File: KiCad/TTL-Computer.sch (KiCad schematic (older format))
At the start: 0 parts

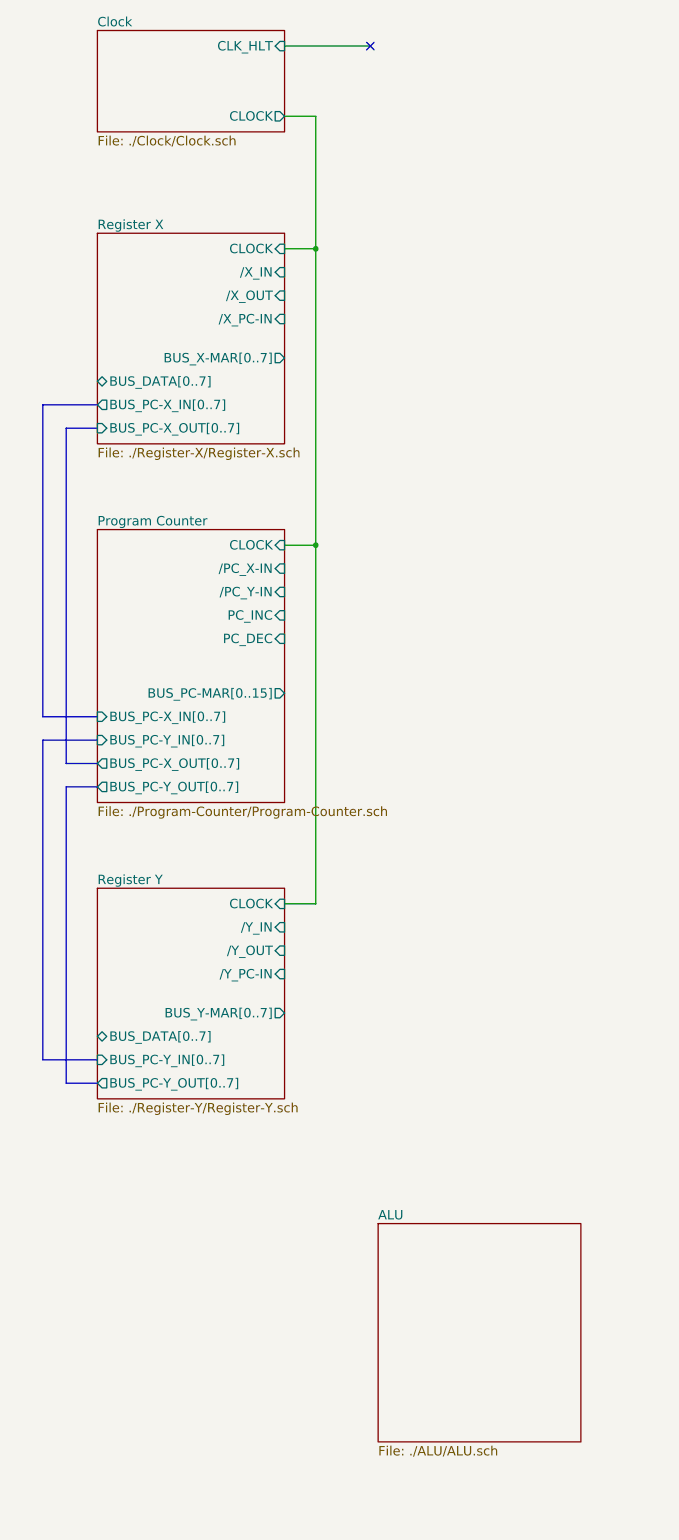
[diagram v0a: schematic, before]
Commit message: Copied X register to Y register
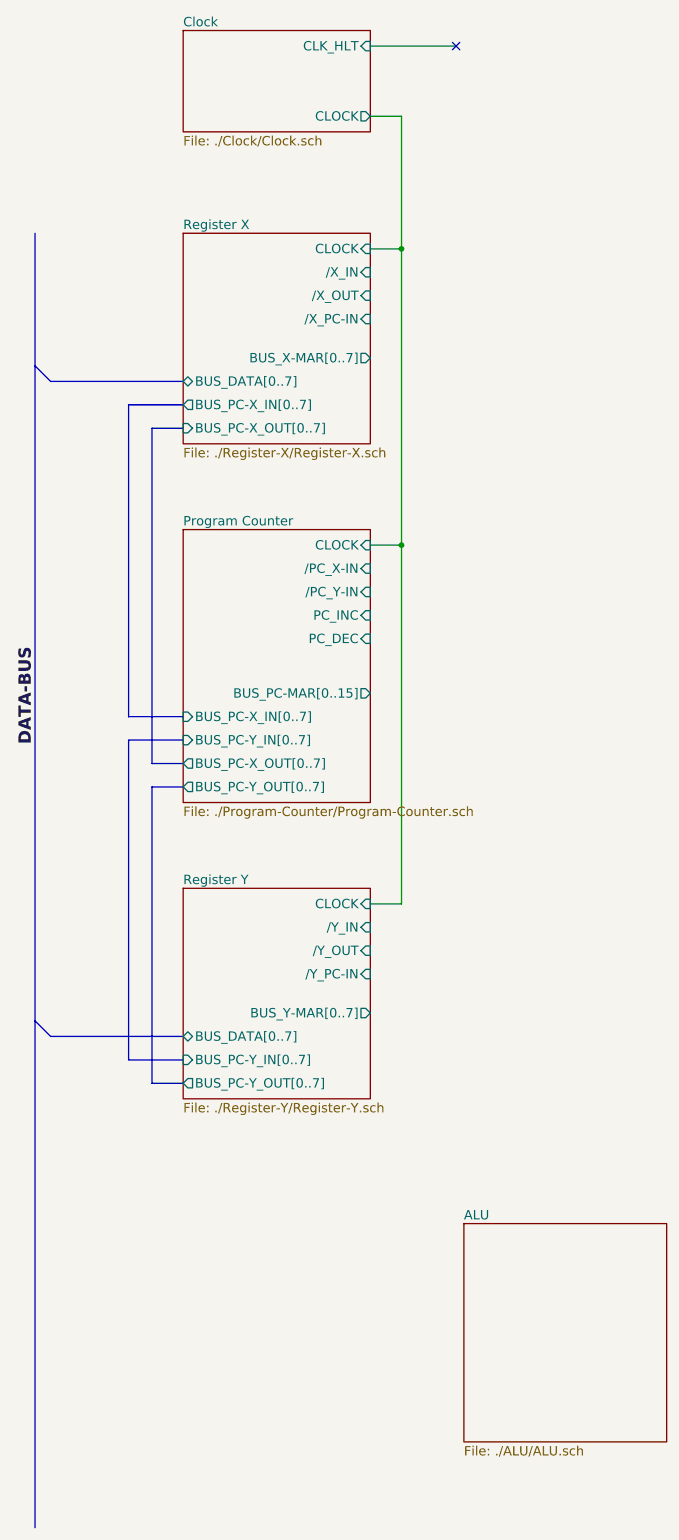
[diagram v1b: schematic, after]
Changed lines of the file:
@@
 $EndDescr
 $Sheet
-S 1100 800  1200 650
+S 1650 800  1200 650
 U 5ACF3206
 F0 "Clock" 60
 F1 "./Clock/Clock.sch" 60
-F2 "CLOCK" O R 2300 1350 60
-F3 "CLK_HLT" I R 2300 900 60
+F2 "CLOCK" O R 2850 1350 60
+F3 "CLK_HLT" I R 2850 900 60
 $EndSheet
 $Sheet
-S 1100 2100 1200 1350
+S 1650 2100 1200 1350
 U 5ACF2F0F
 F0 "Register X" 60
 F1 "./Register-X/Register-X.sch" 60
-F2 "CLOCK" I R 2300 2200 60
-F3 "/X_IN" I R 2300 2350 60
-F4 "/X_OUT" I R 2300 2500 60
-F5 "/X_PC-IN" I R 2300 2650 60
-F6 "BUS_DATA[0..7]" B L 1100 3050 60
-F7 "BUS_PC-X_OUT[0..7]" I L 1100 3350 60
-F8 "BUS_X-MAR[0..7]" O R 2300 2900 60
-F9 "BUS_PC-X_IN[0..7]" O L 1100 3200 60
+F2 "CLOCK" I R 2850 2200 60
+F3 "/X_IN" I R 2850 2350 60
+F4 "/X_OUT" I R 2850 2500 60
+F5 "/X_PC-IN" I R 2850 2650 60
+F6 "BUS_DATA[0..7]" B L 1650 3050 60
+F7 "BUS_PC-X_OUT[0..7]" I L 1650 3350 60
+F8 "BUS_X-MAR[0..7]" O R 2850 2900 60
+F9 "BUS_PC-X_IN[0..7]" O L 1650 3200 60
 $EndSheet
 Wire Bus Line
-	1100 3350 900  3350
+	1650 3350 1450 3350
 Wire Bus Line
-	900  3350 900  5500
+	1450 3350 1450 5500
 Wire Bus Line
-	900  5500 1100 5500
+	1450 5500 1650 5500
 Wire Wire Line
-	2300 1350 2500 1350
+	2850 1350 3050 1350
 Wire Wire Line
-	2500 1350 2500 6400
+	3050 1350 3050 6400
 Wire Wire Line
-	2500 2200 2300 2200
+	3050 2200 2850 2200
 Wire Wire Line
-	2500 4100 2300 4100
-Connection ~ 2500 2200
+	3050 4100 2850 4100
+Connection ~ 3050 2200
 Wire Bus Line
-	1100 3200 750  3200
+	1650 3200 1300 3200
 Wire Bus Line
-	750  3200 750  5200
+	1300 3200 1300 5200
 Wire Bus Line
-	750  5200 1100 5200
-NoConn ~ 2850 900
+	1300 5200 1650 5200
+NoConn ~ 3400 900
 Wire Wire Line
-	2850 900  2300 900
+	3400 900  2850 900
 $Sheet
-S 1100 6300 1200 1350
+S 1650 6300 1200 1350
 U 5AD0848F
 F0 "Register Y" 60
 F1 "./Register-Y/Register-Y.sch" 60
-F2 "BUS_PC-Y_IN[0..7]" I L 1100 7400 60
-F3 "BUS_DATA[0..7]" B L 1100 7250 60
-F4 "CLOCK" I R 2300 6400 60
-F5 "BUS_Y-MAR[0..7]" O R 2300 7100 60
-F6 "/Y_IN" I R 2300 6550 60
-F7 "/Y_OUT" I R 2300 6700 60
-F8 "/Y_PC-IN" I R 2300 6850 60
-F9 "BUS_PC-Y_OUT[0..7]" O L 1100 7550 60
+F2 "BUS_PC-Y_IN[0..7]" I L 1650 7400 60
+F3 "BUS_DATA[0..7]" B L 1650 7250 60
+F4 "CLOCK" I R 2850 6400 60
+F5 "BUS_Y-MAR[0..7]" O R 2850 7100 60
+F6 "/Y_IN" I R 2850 6550 60
+F7 "/Y_OUT" I R 2850 6700 60
+F8 "/Y_PC-IN" I R 2850 6850 60
+F9 "BUS_PC-Y_OUT[0..7]" O L 1650 7550 60
 $EndSheet
 Wire Bus Line
-	1100 5350 750  5350
+	1650 5350 1300 5350
 Wire Bus Line
-	750  5350 750  7400
+	1300 5350 1300 7400
 Wire Bus Line
-	750  7400 1100 7400
+	1300 7400 1650 7400
 Wire Bus Line
-	1100 5650 900  5650
+	1650 5650 1450 5650
 Wire Bus Line
-	900  5650 900  7550
+	1450 5650 1450 7550
 Wire Bus Line
-	900  7550 1100 7550
+	1450 7550 1650 7550
 $Sheet
-S 1100 4000 1200 1750
+S 1650 4000 1200 1750
 U 5ACF340E
 F0 "Program Counter" 60
 F1 "./Program-Counter/Program-Counter.sch" 60
-F2 "/PC_X-IN" I R 2300 4250 60
-F3 "/PC_Y-IN" I R 2300 4400 60
-F4 "PC_INC" I R 2300 4550 60
-F5 "PC_DEC" I R 2300 4700 60
-F6 "CLOCK" I R 2300 4100 60
-F7 "BUS_PC-X_OUT[0..7]" O L 1100 5500 60
-F8 "BUS_PC-Y_OUT[0..7]" O L 1100 5650 60
-F9 "BUS_PC-MAR[0..15]" O R 2300 5050 60
-F10 "BUS_PC-X_IN[0..7]" I L 1100 5200 60
-F11 "BUS_PC-Y_IN[0..7]" I L 1100 5350 60
+F2 "/PC_X-IN" I R 2850 4250 60
+F3 "/PC_Y-IN" I R 2850 4400 60
+F4 "PC_INC" I R 2850 4550 60
+F5 "PC_DEC" I R 2850 4700 60
+F6 "CLOCK" I R 2850 4100 60
+F7 "BUS_PC-X_OUT[0..7]" O L 1650 5500 60
+F8 "BUS_PC-Y_OUT[0..7]" O L 1650 5650 60
+F9 "BUS_PC-MAR[0..15]" O R 2850 5050 60
+F10 "BUS_PC-X_IN[0..7]" I L 1650 5200 60
+F11 "BUS_PC-Y_IN[0..7]" I L 1650 5350 60
 $EndSheet
 Wire Wire Line
-	2500 6400 2300 6400
-Connection ~ 2500 4100
+	3050 6400 2850 6400
+Connection ~ 3050 4100
 $Sheet
-S 2900 8450 1300 1400
+S 3450 8450 1300 1400
 U 5AD5CFF9
 F0 "ALU" 60
 F1 "./ALU/ALU.sch" 60
 $EndSheet
+Wire Bus Line
+	700  2100 700  10400
+Entry Bus Bus
+	700  7150 800  7250
+Wire Bus Line
+	800  7250 1650 7250
+Entry Bus Bus
+	700  2950 800  3050
+Wire Bus Line
+	800  3050 1650 3050
+Text Label 700  4750 3    79   ~ 16
+DATA-BUS
 $EndSCHEMATC

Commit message: Figured out the truth table for my ALU
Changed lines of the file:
@@
 Connection ~ 3050 4100
 $Sheet
-S 3450 8450 1300 1400
+S 3950 8300 1350 2350
 U 5AD5CFF9
 F0 "ALU" 60
 F1 "./ALU/ALU.sch" 60
+F2 "ALU_Cn" I R 5300 8400 60
+F3 "ALU_M" I R 5300 8550 60
+F4 "BUS_A-ALU[0..7]" I L 3950 10400 60
+F5 "BUS_B-ALU[0..7]" I L 3950 10550 60
+F6 "ALU_S0" I R 5300 8700 60
+F7 "ALU_S1" I R 5300 8850 60
+F8 "ALU_S2" I R 5300 9000 60
+F9 "ALU_S3" I R 5300 9150 60
+F10 "ALU_F-EQ" O L 3950 9450 60
+F11 "ALU_F-LT" O L 3950 9600 60
+F12 "ALU_F-GT" O L 3950 9750 60
+F13 "/ALU_OUT" I R 5300 9300 60
+F14 "BUS_DATA[0..7]" O L 3950 10250 60
+F15 "ALU_F-Z" O L 3950 9900 60
+F16 "ALU_F-C" O L 3950 10050 60
 $EndSheet
 Wire Bus Line

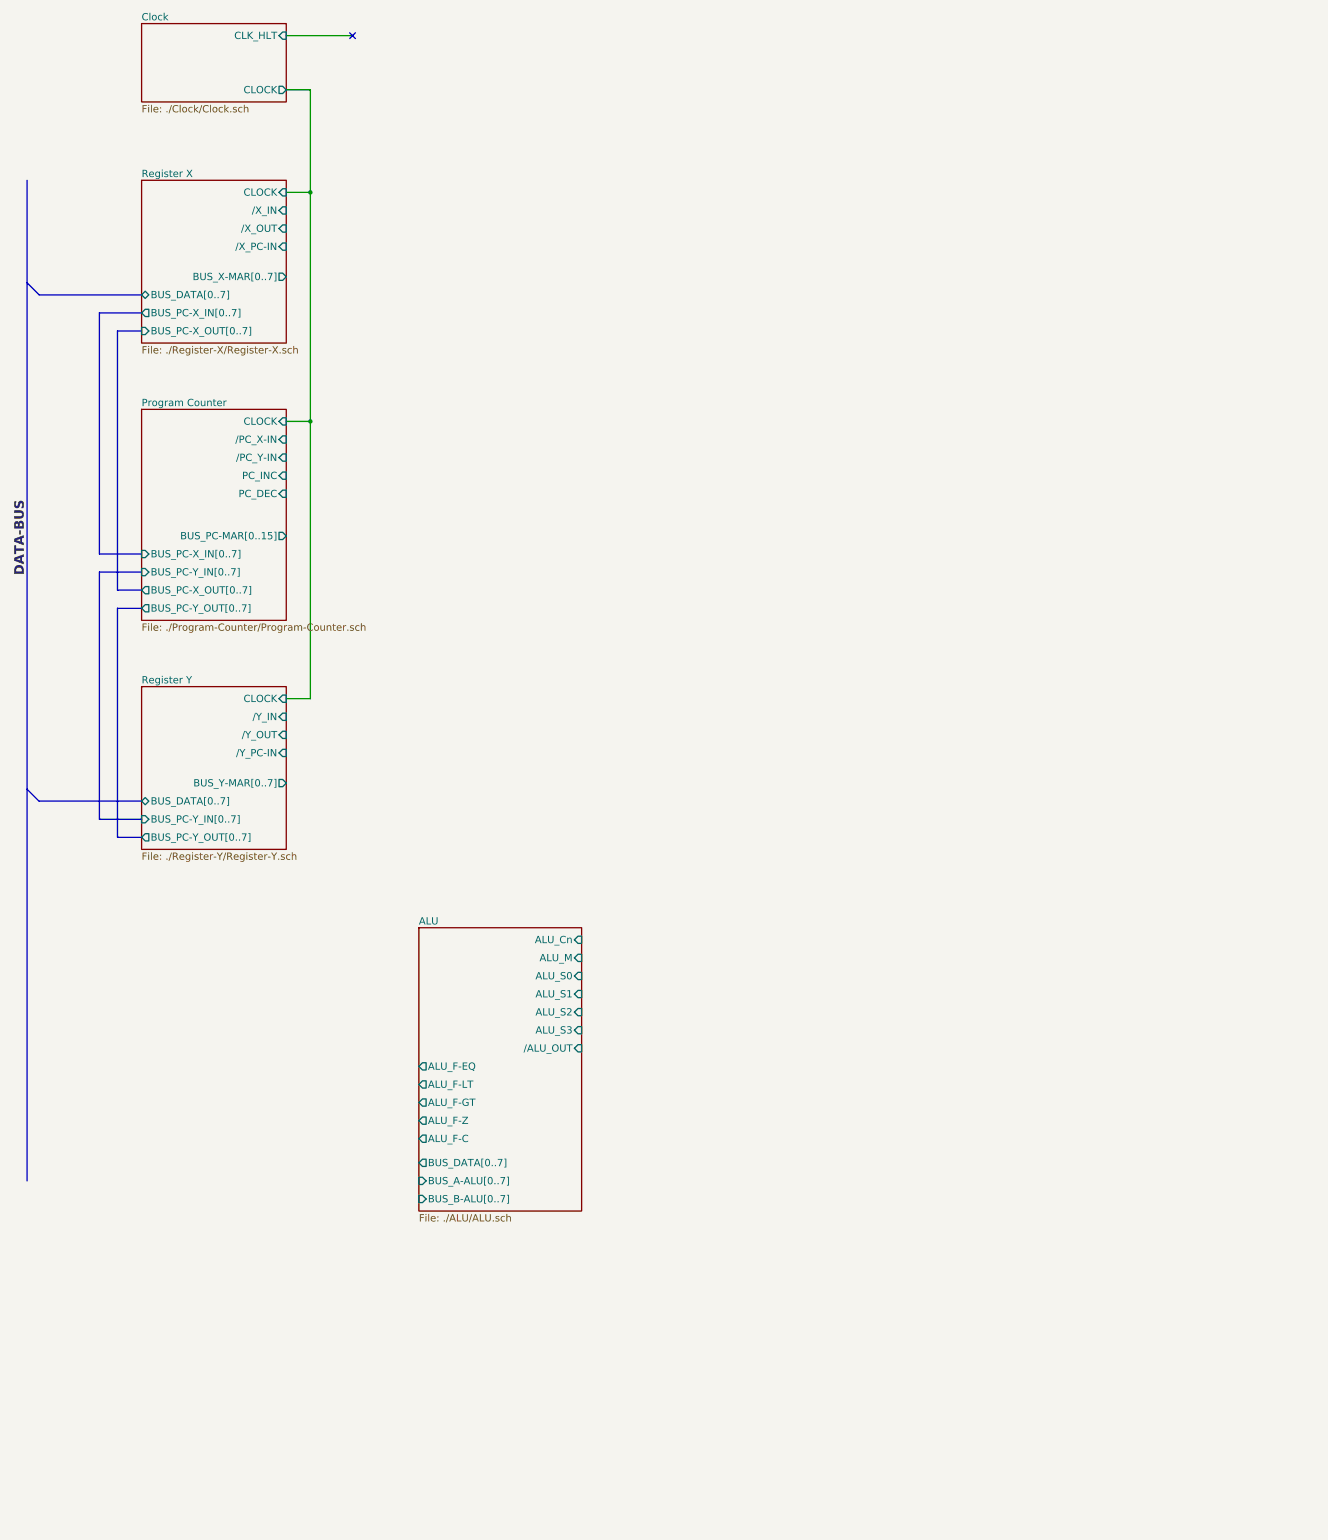
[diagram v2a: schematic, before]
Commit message: Added A and B register schematic
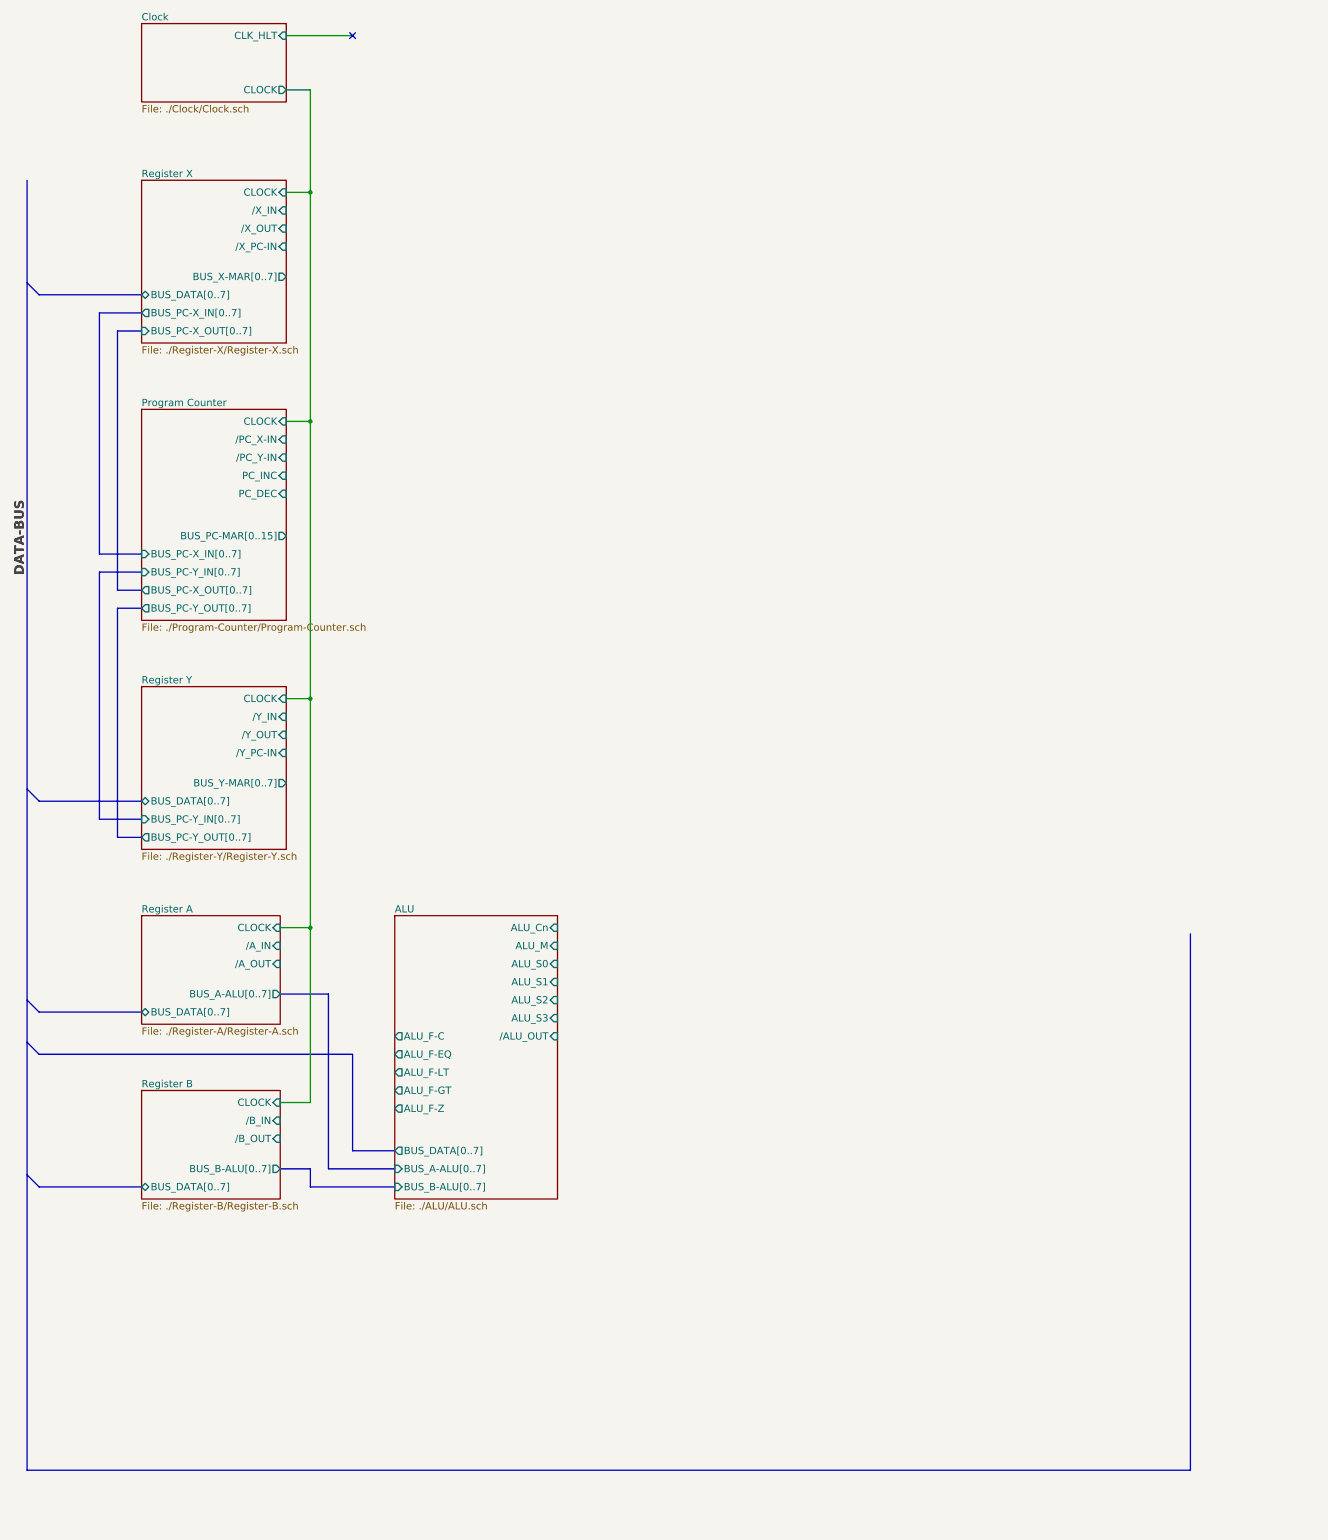
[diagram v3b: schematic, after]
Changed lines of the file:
@@
 $Descr A3 11693 16535 portrait
 encoding utf-8
-Sheet 1 6
+Sheet 1 8
 Title ""
 Date ""
@@
 F9 "BUS_PC-X_IN[0..7]" O L 1650 3200 60
 $EndSheet
-Wire Bus Line
-	1650 3350 1450 3350
-Wire Bus Line
-	1450 3350 1450 5500
-Wire Bus Line
-	1450 5500 1650 5500
-Wire Wire Line
-	2850 1350 3050 1350
-Wire Wire Line
-	3050 1350 3050 6400
-Wire Wire Line
-	3050 2200 2850 2200
-Wire Wire Line
-	3050 4100 2850 4100
-Connection ~ 3050 2200
-Wire Bus Line
-	1650 3200 1300 3200
-Wire Bus Line
-	1300 3200 1300 5200
-Wire Bus Line
-	1300 5200 1650 5200
 NoConn ~ 3400 900
-Wire Wire Line
-	3400 900  2850 900
 $Sheet
 S 1650 6300 1200 1350
@@
 F9 "BUS_PC-Y_OUT[0..7]" O L 1650 7550 60
 $EndSheet
-Wire Bus Line
-	1650 5350 1300 5350
-Wire Bus Line
-	1300 5350 1300 7400
-Wire Bus Line
-	1300 7400 1650 7400
-Wire Bus Line
-	1650 5650 1450 5650
-Wire Bus Line
-	1450 5650 1450 7550
-Wire Bus Line
-	1450 7550 1650 7550
 $Sheet
 S 1650 4000 1200 1750
@@
 F11 "BUS_PC-Y_IN[0..7]" I L 1650 5350 60
 $EndSheet
+$Sheet
+S 3750 8200 1350 2350
+U 5AD5CFF9
+F0 "ALU" 60
+F1 "./ALU/ALU.sch" 60
+F2 "ALU_Cn" I R 5100 8300 60
+F3 "ALU_M" I R 5100 8450 60
+F4 "BUS_A-ALU[0..7]" I L 3750 10300 60
+F5 "BUS_B-ALU[0..7]" I L 3750 10450 60
+F6 "ALU_S0" I R 5100 8600 60
+F7 "ALU_S1" I R 5100 8750 60
+F8 "ALU_S2" I R 5100 8900 60
+F9 "ALU_S3" I R 5100 9050 60
+F10 "ALU_F-EQ" O L 3750 9350 60
+F11 "ALU_F-LT" O L 3750 9500 60
+F12 "ALU_F-GT" O L 3750 9650 60
+F13 "/ALU_OUT" I R 5100 9200 60
+F14 "BUS_DATA[0..7]" O L 3750 10150 60
+F15 "ALU_F-Z" O L 3750 9800 60
+F16 "ALU_F-C" O L 3750 9200 60
+$EndSheet
+Entry Bus Bus
+	700  7150 800  7250
+Entry Bus Bus
+	700  2950 800  3050
+Text Label 700  4750 3    79   ~ 16
+DATA-BUS
+$Sheet
+S 1650 9650 1150 900
+U 5AEB52B5
+F0 "Register B" 60
+F1 "./Register-B/Register-B.sch" 60
+F2 "/B_OUT" I R 2800 10050 60
+F3 "CLOCK" I R 2800 9750 60
+F4 "BUS_DATA[0..7]" B L 1650 10450 60
+F5 "BUS_B-ALU[0..7]" O R 2800 10300 60
+F6 "/B_IN" I R 2800 9900 60
+$EndSheet
+Wire Bus Line
+	1650 3350 1450 3350
+Wire Bus Line
+	1450 3350 1450 5500
+Wire Bus Line
+	1450 5500 1650 5500
+Wire Wire Line
+	2850 1350 3050 1350
+Wire Wire Line
+	3050 1350 3050 9750
+Wire Wire Line
+	3050 2200 2850 2200
+Wire Wire Line
+	3050 4100 2850 4100
+Connection ~ 3050 2200
+Wire Bus Line
+	1650 3200 1300 3200
+Wire Bus Line
+	1300 3200 1300 5200
+Wire Bus Line
+	1300 5200 1650 5200
+Wire Wire Line
+	3400 900  2850 900
+Wire Bus Line
+	1650 5350 1300 5350
+Wire Bus Line
+	1300 5350 1300 7400
+Wire Bus Line
+	1300 7400 1650 7400
+Wire Bus Line
+	1650 5650 1450 5650
+Wire Bus Line
+	1450 5650 1450 7550
+Wire Bus Line
+	1450 7550 1650 7550
 Wire Wire Line
 	3050 6400 2850 6400
 Connection ~ 3050 4100
-$Sheet
-S 3950 8300 1350 2350
-U 5AD5CFF9
-F0 "ALU" 60
-F1 "./ALU/ALU.sch" 60
-F2 "ALU_Cn" I R 5300 8400 60
-F3 "ALU_M" I R 5300 8550 60
-F4 "BUS_A-ALU[0..7]" I L 3950 10400 60
-F5 "BUS_B-ALU[0..7]" I L 3950 10550 60
-F6 "ALU_S0" I R 5300 8700 60
-F7 "ALU_S1" I R 5300 8850 60
-F8 "ALU_S2" I R 5300 9000 60
-F9 "ALU_S3" I R 5300 9150 60
-F10 "ALU_F-EQ" O L 3950 9450 60
-F11 "ALU_F-LT" O L 3950 9600 60
-F12 "ALU_F-GT" O L 3950 9750 60
-F13 "/ALU_OUT" I R 5300 9300 60
-F14 "BUS_DATA[0..7]" O L 3950 10250 60
-F15 "ALU_F-Z" O L 3950 9900 60
-F16 "ALU_F-C" O L 3950 10050 60
-$EndSheet
 Wire Bus Line
-	700  2100 700  10400
-Entry Bus Bus
-	700  7150 800  7250
+	700  2100 700  12800
 Wire Bus Line
 	800  7250 1650 7250
-Entry Bus Bus
-	700  2950 800  3050
 Wire Bus Line
 	800  3050 1650 3050
-Text Label 700  4750 3    79   ~ 16
-DATA-BUS
+Entry Bus Bus
+	700  8900 800  9000
+Wire Bus Line
+	700  12800 10350 12800
+Wire Bus Line
+	10350 12800 10350 8350
+Entry Bus Bus
+	700  10350 800  10450
+Wire Bus Line
+	800  9000 1650 9000
+Wire Bus Line
+	800  10450 1650 10450
+Wire Wire Line
+	3050 8300 2800 8300
+Connection ~ 3050 6400
+$Sheet
+S 1650 8200 1150 900
+U 5AEB1288
+F0 "Register A" 60
+F1 "./Register-A/Register-A.sch" 60
+F2 "/A_OUT" I R 2800 8600 60
+F3 "CLOCK" I R 2800 8300 60
+F4 "BUS_DATA[0..7]" B L 1650 9000 60
+F5 "BUS_A-ALU[0..7]" O R 2800 8850 60
+F6 "/A_IN" I R 2800 8450 60
+$EndSheet
+Wire Wire Line
+	3050 9750 2800 9750
+Connection ~ 3050 8300
+Wire Bus Line
+	2800 10300 3050 10300
+Wire Bus Line
+	3050 10300 3050 10450
+Wire Bus Line
+	3050 10450 3750 10450
+Wire Bus Line
+	2800 8850 3200 8850
+Wire Bus Line
+	3200 8850 3200 10300
+Wire Bus Line
+	3200 10300 3750 10300
+Entry Bus Bus
+	700  9250 800  9350
+Wire Bus Line
+	800  9350 3400 9350
+Wire Bus Line
+	3400 9350 3400 10150
+Wire Bus Line
+	3400 10150 3750 10150
 $EndSCHEMATC

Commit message: Added some schematics
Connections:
- no-connect marks 1 -> 3
